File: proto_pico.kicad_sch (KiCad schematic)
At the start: 105 parts, among them J1 USB-C Receptacle, J11 Header_2.54mm_1x5, J16 Header_2.54mm_1x5, J2 Screw_Terminal_01x02, J3 Screw_Terminal_01x02, J4 Screw_Terminal_01x02, J6 Header_2.54mm_1x7, J8 Header_2.54mm_1x5, SW1 PTS647, SW2 PTS647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

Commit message: done some routing
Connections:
- net HB_DIRECTION_A: now also J11.4; no longer J11.5
- net HB_DIRECTION_B: now also J11.2; no longer J11.3
- net HB_ENABLE_A: now also J11.3; no longer J11.4
- net HB_ENABLE_B: now also J11.1; no longer J11.2
- net HB_MODE: now also J11.5
- net LRCLK_AUDIO: now also J6.2; no longer J6.4
- net MCLK_AUDIO: now also J6.1; no longer J6.3
- net SCL: now also J6.3; no longer J6.1
- net SCLK_AUDIO: now also J6.7; no longer J6.5
- net SDA: now also J6.4; no longer J6.2
- net SDI_AUDIO: now also J6.6; no longer J6.7
- net SDO_AUDIO: now also J6.5; no longer J6.6
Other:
- moved on the sheet: J6

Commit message: some updates to schematic and component placement
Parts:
- added J17: ~, Connectors:PinHeader_1x02_P2.54mm_Vertical, symbol Connectors:Header_2.54mm_1x2
- added U10: 74LVC1G17, symbol 74xGxx:74LVC1G17
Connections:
- net +3V3: now also U10.5 (VCC)
- net GND: now also J17.2 (Pin_2), U10.3 (GND)
- net MIC_D7: now also U10.2
- new net: J17.1 (Pin_1), U10.4
- no-connect marks 29 -> 30
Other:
- moved on the sheet: J15

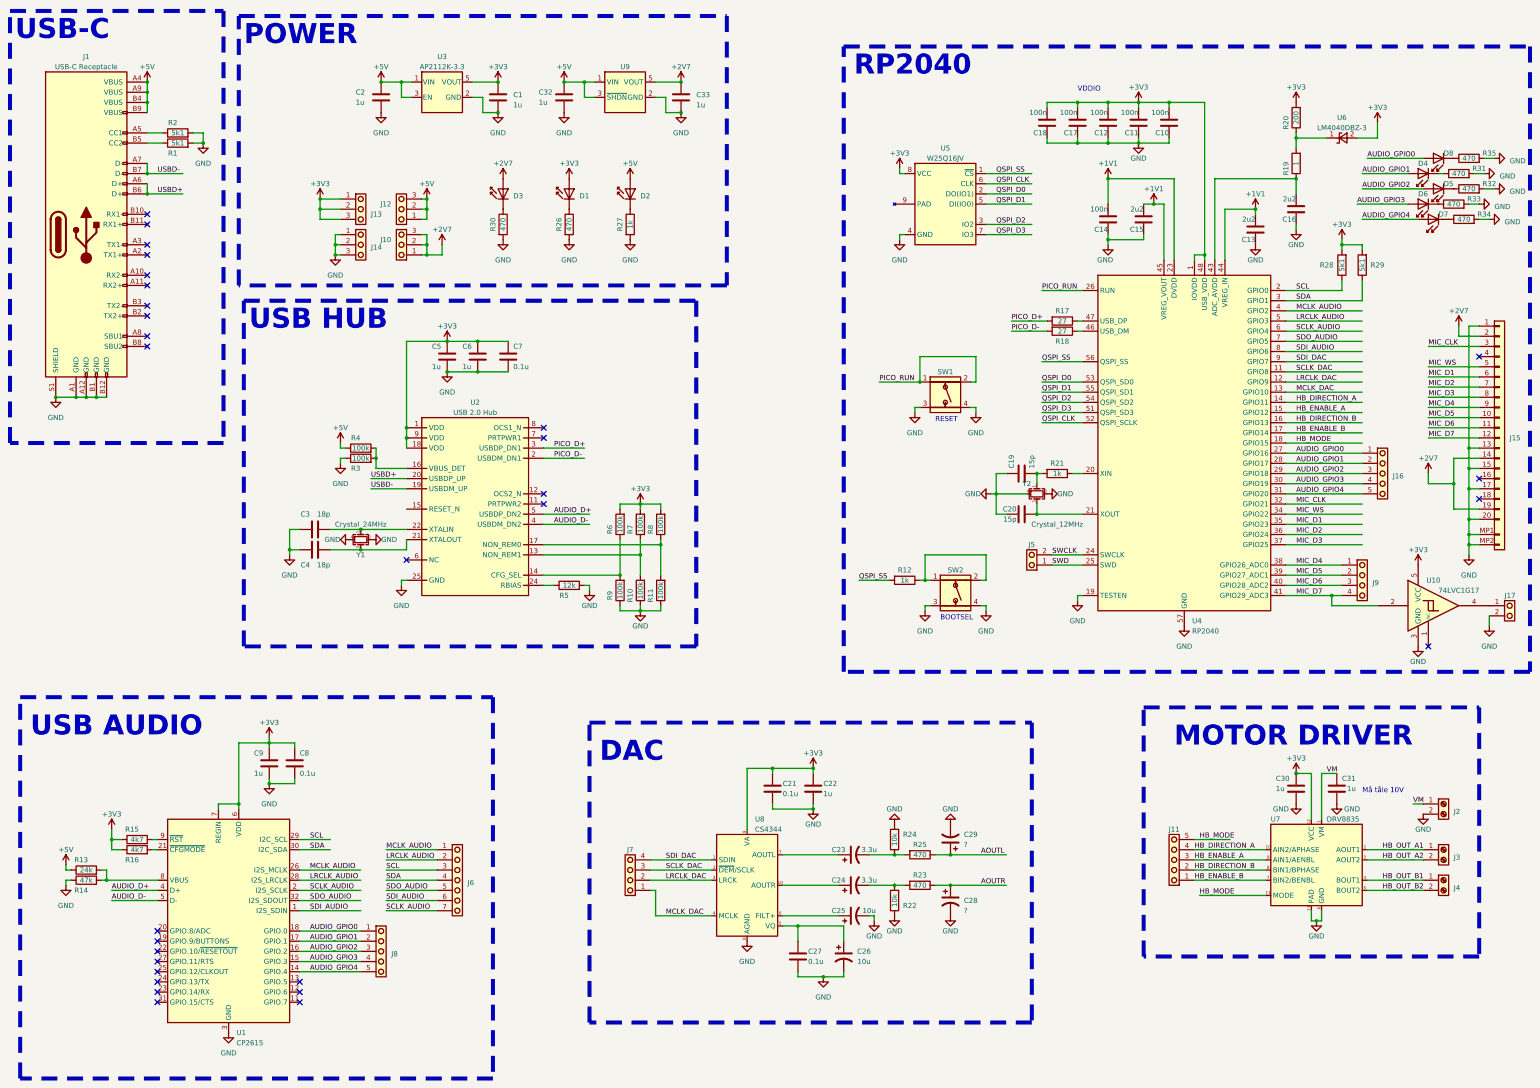
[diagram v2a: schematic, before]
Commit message: routing done, DRC left
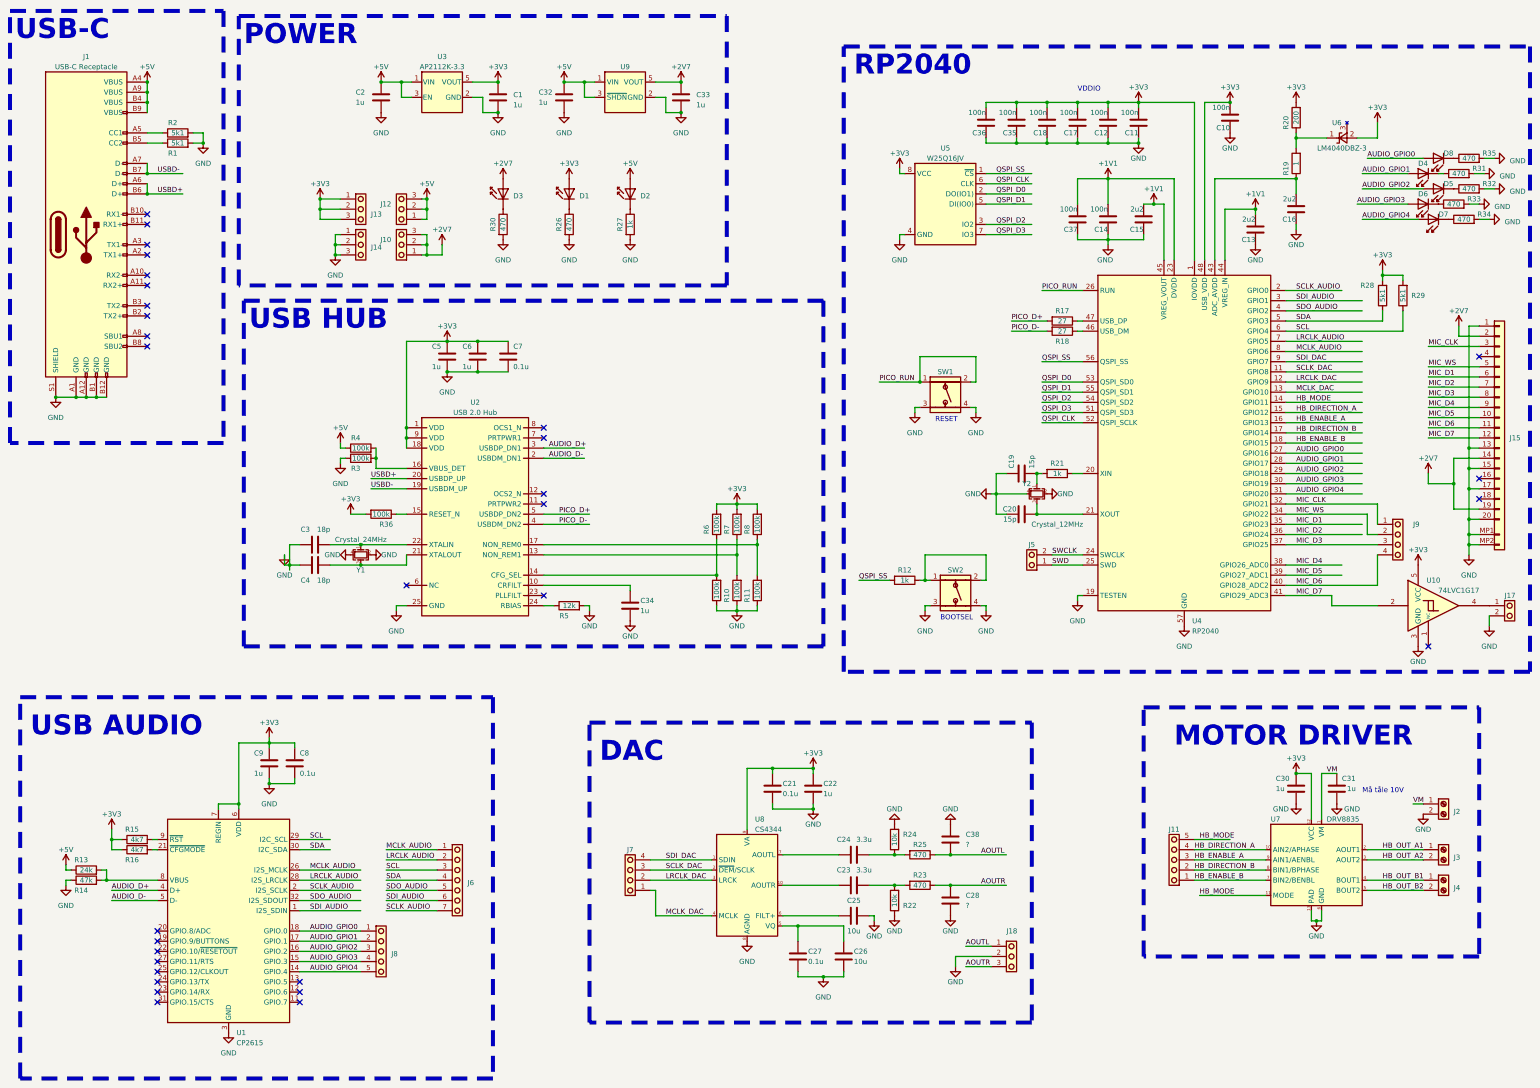
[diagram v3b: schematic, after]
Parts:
- removed C23, C24: 3.3u, Capasitors:CP_Elec_10x10, symbol Capacitors:C_Aluminius_10.3mm
- removed C25, C26: 10u, Capasitors:CP_Elec_10x10, symbol Capacitors:C_Aluminius_10.3mm
- removed C28, C29: ?, Capasitors:CP_Elec_10x10, symbol Capacitors:C_Aluminius_10.3mm
- removed J16: Header_2.54mm_1x5, Connectors:PinHeader_1x05_P2.54mm_Vertical, symbol Connectors:Header_2.54mm_1x5
- added C23, C24: 3.3u, Capasitors:C_0805_2012Metric, symbol Capacitors.kicad_sym:C_Ceramic_0804
- added C25, C26: 10u, Capasitors:C_0805_2012Metric, symbol Capacitors.kicad_sym:C_Ceramic_0804
- added C28, C38: ?, Capasitors:C_0805_2012Metric, symbol Capacitors.kicad_sym:C_Ceramic_0804
- added C34: 1u, Capasitors:C_0603_1608Metric, symbol Capacitors:C_Ceramic_0603
- added C35, C36, C37: 100n, Capasitors:C_0603_1608Metric, symbol Capacitors:C_Ceramic_0603
- added J18: ~, Connectors:PinHeader_1x03_P2.54mm_Vertical, symbol Connectors:Header_2.54mm_1x3
- added R36: 100k, Resistor_SMD:R_0603_1608Metric, symbol Resistors:R_0603
- U10: footprint (none) -> Package_TO_SOT_SMD:SOT-23-5
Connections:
- net +1V1: now also C37.2
- net +3V3: now also C35.2, C36.2, R36.2
- net AOUTL: now also C38.2, J18.1 (Pin_1)
- net AOUTR: now also C28.1, J18.3 (Pin_3)
- net AUDIO_D+: now also U2.3 (USBDP_DN1); no longer U2.5 (USBDP_DN2)
- net AUDIO_D-: now also U2.2 (USBDM_DN1); no longer U2.4 (USBDM_DN2)
- net GND: now also C25.2, C26.2, C28.2, C34.2, C35.1, C36.1, C37.1, C38.1, J18.2 (Pin_2)
- net HB_DIRECTION_A: now also U4.15 (GPIO12); no longer U4.14 (GPIO11)
- net HB_DIRECTION_B: now also U4.17 (GPIO14); no longer U4.16 (GPIO13)
- net HB_ENABLE_A: now also U4.16 (GPIO13); no longer U4.15 (GPIO12)
- net HB_ENABLE_B: now also U4.18 (GPIO15); no longer U4.17 (GPIO14)
- net HB_MODE: now also U4.14 (GPIO11); no longer U4.18 (GPIO15)
- net LRCLK_AUDIO: now also U4.7 (GPIO5); no longer U4.5 (GPIO3)
- net MCLK_AUDIO: now also U4.8 (GPIO6); no longer U4.4 (GPIO2)
- net MIC_CLK: now also J9.1
- net MIC_D3: now also J9.3
- net MIC_D4: no longer J9.1
- net MIC_D5: no longer J9.2
- net MIC_D6: now also J9.4; no longer J9.3
- net MIC_D7: no longer J9.4
- net MIC_WS: now also J9.2
- net PICO_D+: now also U2.5 (USBDP_DN2); no longer U2.3 (USBDP_DN1)
- net PICO_D-: now also U2.4 (USBDM_DN2); no longer U2.2 (USBDM_DN1)
- net SCL: now also R29.1, U4.6 (GPIO4); no longer R28.1, U4.2 (GPIO0)
- net SCLK_AUDIO: now also U4.2 (GPIO0); no longer U4.6 (GPIO4)
- net SDA: now also R28.1, U4.5 (GPIO3); no longer R29.1, U4.3 (GPIO1)
- net SDI_AUDIO: now also U4.3 (GPIO1); no longer U4.8 (GPIO6)
- net SDO_AUDIO: now also U4.4 (GPIO2); no longer U4.7 (GPIO5)
- net at R24.1, R25.2: now also C24.1
- net at C27.1, U8.5 (VQ): now also C26.1
- net at U8.6 (FILT+): now also C25.1
- net at U8.10 (AOUTR): now also C23.1
- net at R22.2, R23.2: now also C23.2
- net at U8.7 (AOUTL): now also C24.2
- net at U2.15 (RESET_N): now also R36.1
- new net: C34.1, U2.10 (CRFILT)
- no-connect marks 30 -> 31
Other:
- moved on the sheet: C3, C4, R10, R11, R28, R29, R6, R7, R8, Y1
